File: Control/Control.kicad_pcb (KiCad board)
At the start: 2 copper layers, 144.8 x 73.9 mm, 68 parts, among them J1 Conn_01x03_Pin, J2 Conn_01x04_Pin, J3 Conn_01x08_Pin, J4 Conn_01x08_Pin, J5 Conn_01x07_Pin, SW1 SW_MEC_5E, U1 AT28C64B-15PI, U2 AT28C64B-15PI, U3 SN74AC14N, U4 SN74AC14N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

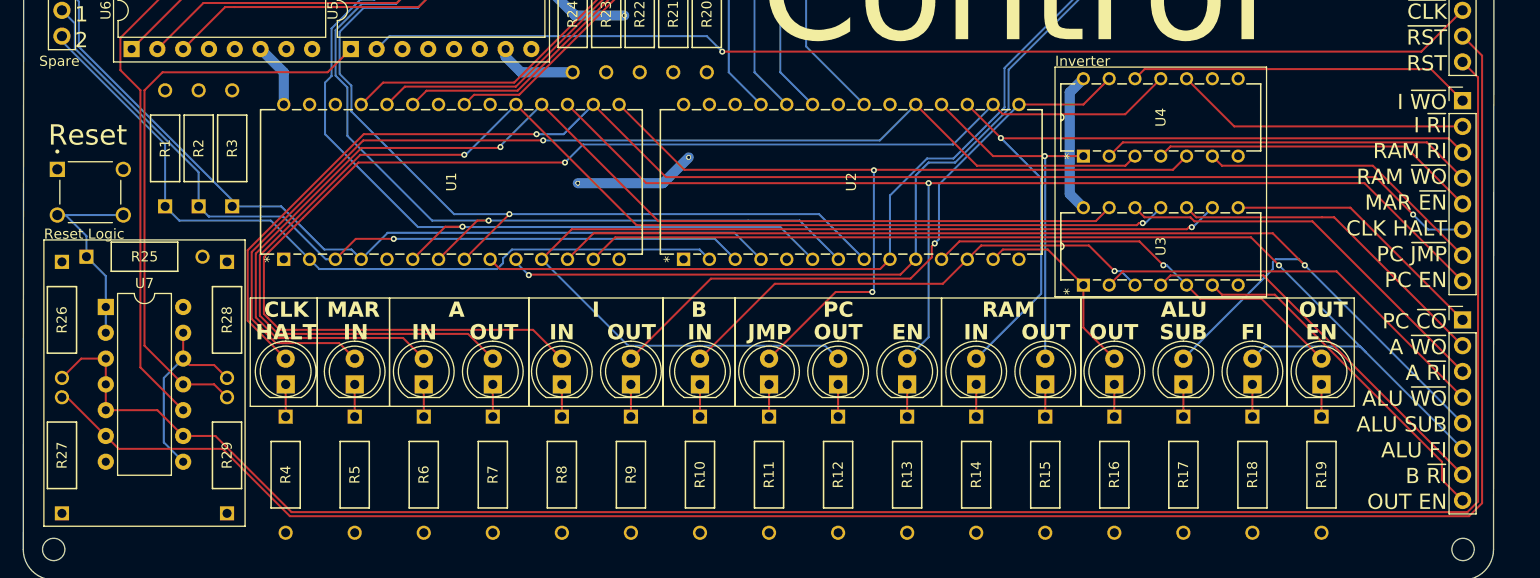
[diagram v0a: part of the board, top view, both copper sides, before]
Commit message: Control reset signals were inverted
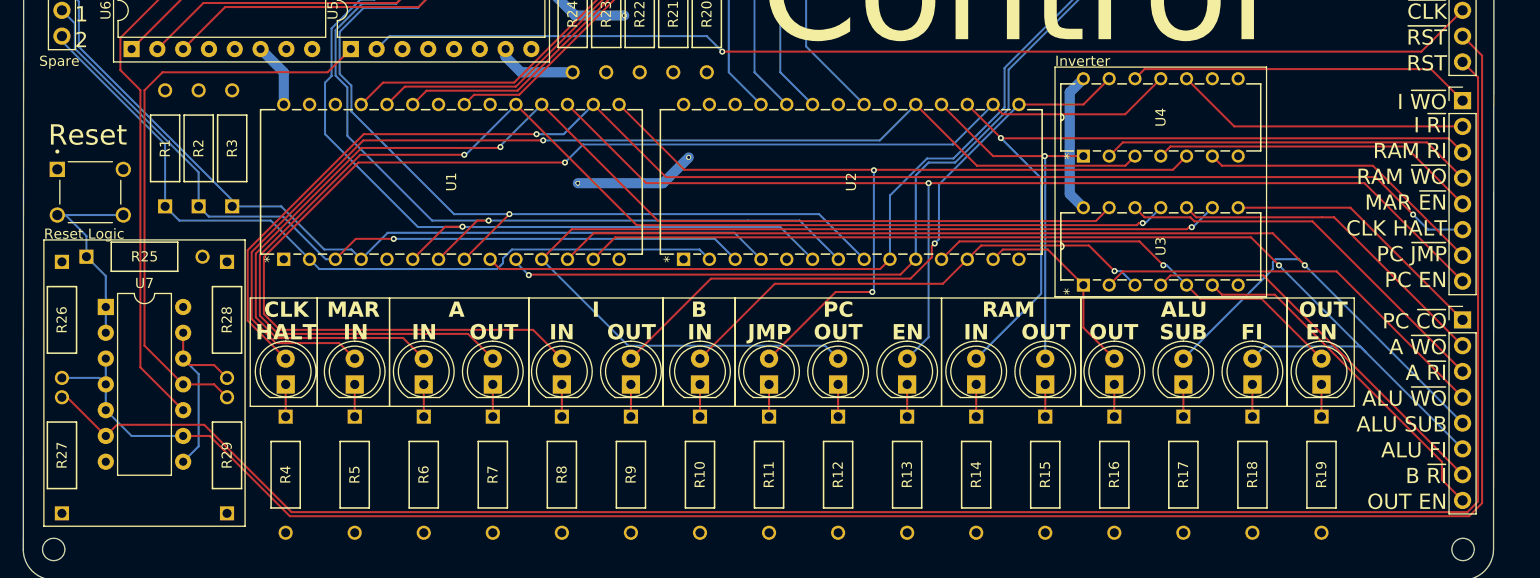
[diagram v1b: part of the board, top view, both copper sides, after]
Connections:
- R26 pad 2: /RST -> /~{RST}
- R27 pad 2: /~{RST} -> /RST
- U7 pad 3: /RST -> /~{RST}
- U7 pad 4: /RST -> /~{RST}
- U7 pad 5: /RST -> /~{RST}
- U7 pad 6: /~{RST} -> /RST
- U7 pad 9: /RST -> /~{RST}
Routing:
- net /~{RST}: track 192.0 -> 196.8 mm
- net /RST: track 193.8 -> 189.4 mm
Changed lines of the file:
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@@
 			(layers "*.Cu" "*.Mask")
 			(remove_unused_layers no)
-			(net 59 "/RST")
+			(net 57 "/~{RST}")
 			(pintype "passive")
 		)
@@
 			(layers "*.Cu" "*.Mask")
 			(remove_unused_layers no)
-			(net 57 "/~{RST}")
+			(net 59 "/RST")
 			(pintype "passive")
 		)
@@
 			(layers "*.Cu" "*.Mask")
 			(remove_unused_layers no)
-			(net 59 "/RST")
+			(net 57 "/~{RST}")
 			(pintype "output")
 		)
@@
 			(layers "*.Cu" "*.Mask")
 			(remove_unused_layers no)
-			(net 59 "/RST")
+			(net 57 "/~{RST}")
 			(pintype "input")
 		)
@@
 			(layers "*.Cu" "*.Mask")
 			(remove_unused_layers no)
-			(net 59 "/RST")
+			(net 57 "/~{RST}")
 			(pintype "input")
 		)
@@
 			(layers "*.Cu" "*.Mask")
 			(remove_unused_layers no)
-			(net 57 "/~{RST}")
+			(net 59 "/RST")
 			(pintype "output")
 		)
@@
 			(layers "*.Cu" "*.Mask")
 			(remove_unused_layers no)
-			(net 59 "/RST")
+			(net 57 "/~{RST}")
 			(pintype "input")
 		)
@@
 	)
 	(segment
-		(start 196.730032 145.314)
-		(end 80.613314 145.314)
+		(start 196.088 98.044)
+		(end 198.012 99.968)
 		(width 0.2)
 		(layer "F.Cu")
@@
 	)
 	(segment
-		(start 196.088 98.044)
-		(end 198.012 99.968)
+		(start 198.012 144.032032)
+		(end 196.730032 145.314)
 		(width 0.2)
 		(layer "F.Cu")
@@
 	(segment
 		(start 80.613314 145.314)
-		(end 73.983314 138.684)
+		(end 72.713314 137.414)
 		(width 0.2)
 		(layer "F.Cu")
@@
 	)
 	(segment
-		(start 198.012 99.968)
-		(end 198.012 144.032032)
+		(start 72.713314 137.414)
+		(end 70.104 137.414)
 		(width 0.2)
 		(layer "F.Cu")
@@
 	)
 	(segment
-		(start 73.983314 138.684)
-		(end 63.754 138.684)
+		(start 196.730032 145.314)
+		(end 80.613314 145.314)
 		(width 0.2)
 		(layer "F.Cu")
@@
 	)
 	(segment
-		(start 198.012 144.032032)
-		(end 196.730032 145.314)
+		(start 198.012 99.968)
+		(end 198.012 144.032032)
 		(width 0.2)
 		(layer "F.Cu")
@@
 	)
 	(segment
-		(start 63.754 138.684)
-		(end 62.484 137.414)
+		(start 61.849 131.699)
+		(end 62.484 132.334)
 		(width 0.2)
-		(layer "F.Cu")
+		(layer "B.Cu")
 		(net 57)
 	)
 	(segment
-		(start 62.484 137.414)
-		(end 58.674 133.604)
+		(start 58.166 131.699)
+		(end 61.849 131.699)
 		(width 0.2)
-		(layer "F.Cu")
+		(layer "B.Cu")
 		(net 57)
 	)
 	(segment
-		(start 58.674 133.604)
-		(end 58.166 133.604)
+		(start 65.024 137.414)
+		(end 62.484 134.874)
 		(width 0.2)
-		(layer "F.Cu")
+		(layer "B.Cu")
+		(net 57)
+	)
+	(segment
+		(start 62.484 132.334)
+		(end 62.484 129.794)
+		(width 0.2)
+		(layer "B.Cu")
+		(net 57)
+	)
+	(segment
+		(start 62.484 134.874)
+		(end 62.484 132.334)
+		(width 0.2)
+		(layer "B.Cu")
+		(net 57)
+	)
+	(segment
+		(start 70.104 137.414)
+		(end 65.024 137.414)
+		(width 0.2)
+		(layer "B.Cu")
 		(net 57)
 	)
@@
 	)
 	(segment
-		(start 62.484 132.334)
-		(end 62.484 134.874)
+		(start 196.088 100.584)
+		(end 197.612 102.108)
 		(width 0.2)
 		(layer "F.Cu")
@@
 	)
 	(segment
-		(start 67.564 134.874)
-		(end 70.104 137.414)
+		(start 80.779 144.914)
+		(end 72.179 136.314)
 		(width 0.2)
 		(layer "F.Cu")
@@
 	)
 	(segment
-		(start 60.071 129.794)
-		(end 62.484 129.794)
+		(start 63.584 136.314)
+		(end 62.484 137.414)
 		(width 0.2)
 		(layer "F.Cu")
@@
 	(segment
 		(start 196.564346 144.914)
-		(end 197.612 143.866346)
-		(width 0.2)
-		(layer "F.Cu")
-		(net 59)
-	)
-	(segment
-		(start 62.484 129.794)
-		(end 62.484 132.334)
-		(width 0.2)
-		(layer "F.Cu")
-		(net 59)
-	)
-	(segment
-		(start 197.612 102.108)
-		(end 196.088 100.584)
+		(end 80.779 144.914)
 		(width 0.2)
 		(layer "F.Cu")
@@
 	)
 	(segment
-		(start 73.279 137.414)
-		(end 70.104 137.414)
-		(width 0.2)
-		(layer "F.Cu")
-		(net 59)
-	)
-	(segment
-		(start 80.779 144.914)
+		(start 197.612 143.866346)
 		(end 196.564346 144.914)
 		(width 0.2)
@@
 	)
 	(segment
-		(start 62.484 134.874)
-		(end 67.564 134.874)
+		(start 197.612 102.108)
+		(end 197.612 143.866346)
 		(width 0.2)
 		(layer "F.Cu")
@@
 	)
 	(segment
-		(start 80.779 144.914)
-		(end 73.279 137.414)
+		(start 58.674 133.604)
+		(end 58.166 133.604)
 		(width 0.2)
 		(layer "F.Cu")
@@
 	)
 	(segment
-		(start 197.612 143.866346)
-		(end 197.612 102.108)
+		(start 72.179 136.314)
+		(end 63.584 136.314)
 		(width 0.2)
 		(layer "F.Cu")
@@
 	)
 	(segment
-		(start 58.166 131.699)
-		(end 60.071 129.794)
+		(start 62.484 137.414)
+		(end 58.674 133.604)
 		(width 0.2)
 		(layer "F.Cu")
@@
 	)
 	(segment
-		(start 70.104 139.954)
-		(end 68.199 138.049)
+		(start 71.628 138.43)
+		(end 71.628 131.318)
 		(width 0.2)
 		(layer "B.Cu")
@@
 	)
 	(segment
-		(start 68.199 138.049)
-		(end 68.199 131.699)
+		(start 70.104 139.954)
+		(end 71.628 138.43)
 		(width 0.2)
 		(layer "B.Cu")
@@
 	)
 	(segment
-		(start 68.199 131.699)
+		(start 71.628 131.318)
 		(end 70.104 129.794)
 		(width 0.2)
